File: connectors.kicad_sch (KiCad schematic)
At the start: 4 parts, among them J1 Conn_01x04_Pin, J2 Conn_01x04_Pin, J3 Conn_01x09_Pin, J4 Conn_02x03_Odd_Even

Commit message: Assigned footprints to the components in EESchema.
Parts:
- J1, J2: footprint (none) -> Connector_PinHeader_2.54mm:PinHeader_1x04_P2.54mm_Vertical
- J3: footprint (none) -> Connector_PinHeader_2.54mm:PinHeader_1x09_P2.54mm_Vertical
- J4: footprint (none) -> Connector_PinHeader_2.54mm:PinHeader_2x03_P2.54mm_Vertical
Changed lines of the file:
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@@
 			)
 		)
-		(property "Footprint" ""
+		(property "Footprint" "Connector_PinHeader_2.54mm:PinHeader_2x03_P2.54mm_Vertical"
 			(at 95.25 58.42 0)
 			(effects
@@
 			)
 		)
-		(property "Footprint" ""
+		(property "Footprint" "Connector_PinHeader_2.54mm:PinHeader_1x04_P2.54mm_Vertical"
 			(at 60.96 31.75 0)
 			(effects
@@
 			)
 		)
-		(property "Footprint" ""
+		(property "Footprint" "Connector_PinHeader_2.54mm:PinHeader_1x04_P2.54mm_Vertical"
 			(at 93.98 31.75 0)
 			(effects
@@
 			)
 		)
-		(property "Footprint" ""
+		(property "Footprint" "Connector_PinHeader_2.54mm:PinHeader_1x09_P2.54mm_Vertical"
 			(at 60.96 60.96 0)
 			(effects

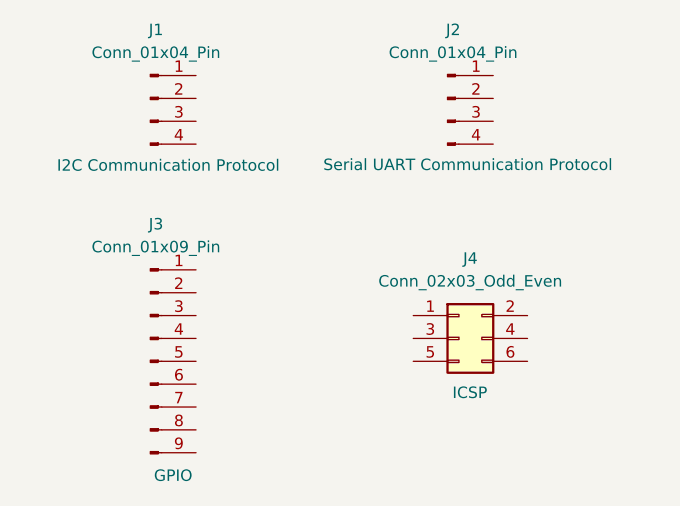
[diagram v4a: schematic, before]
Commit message: Finished the wiring of the schematic.
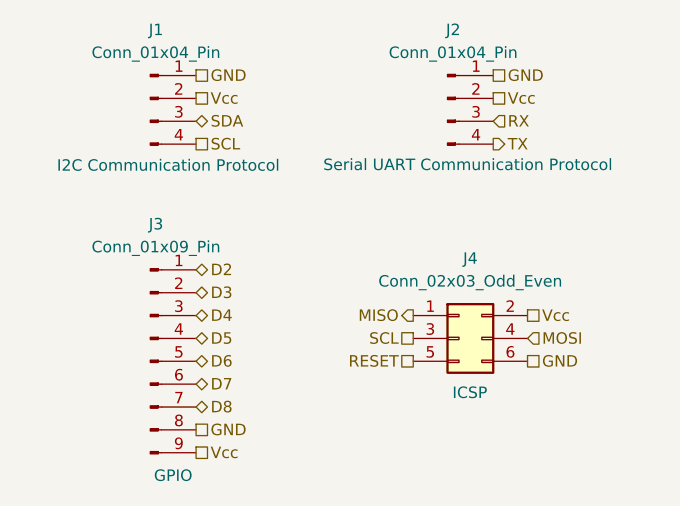
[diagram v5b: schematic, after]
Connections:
- net MISO: now reaches J4.1 (Pin_1)
- net Vcc: now reaches J4.2 (Pin_2)
- net Vcc: now also J1.2 (Pin_2), J2.2 (Pin_2), J3.9 (Pin_9)
- net SCL: now reaches J4.3 (Pin_3)
- net SCL: now also J1.4 (Pin_4)
- net MOSI: now reaches J4.4 (Pin_4)
- net RESET: now reaches J4.5 (Pin_5)
- net GND: now reaches J4.6 (Pin_6)
- net GND: now also J1.1 (Pin_1), J2.1 (Pin_1), J3.8 (Pin_8)
- net SDA: now reaches J1.3 (Pin_3)
- net RX: now reaches J2.3 (Pin_3)
- net TX: now reaches J2.4 (Pin_4)
- net D2: now reaches J3.1 (Pin_1)
- net D3: now reaches J3.2 (Pin_2)
- net D4: now reaches J3.3 (Pin_3)
- net D5: now reaches J3.4 (Pin_4)
- net D6: now reaches J3.5 (Pin_5)
- net D7: now reaches J3.6 (Pin_6)
- net D8: now reaches J3.7 (Pin_7)
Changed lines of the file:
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@@
 	(generator_version "9.0")
 	(paper "A4")
+	(hierarchical_label "D6"
+		(shape bidirectional)
+		(at 66.04 60.96 0)
+		(effects
+			(font
+				(size 1.27 1.27)
+			)
+			(justify left)
+		)
+	)
+	(hierarchical_label "GND"
+		(shape passive)
+		(at 99.06 29.21 0)
+		(effects
+			(font
+				(size 1.27 1.27)
+			)
+			(justify left)
+		)
+	)
+	(hierarchical_label "D2"
+		(shape bidirectional)
+		(at 66.04 50.8 0)
+		(effects
+			(font
+				(size 1.27 1.27)
+			)
+			(justify left)
+		)
+	)
+	(hierarchical_label "GND"
+		(shape passive)
+		(at 66.04 29.21 0)
+		(effects
+			(font
+				(size 1.27 1.27)
+			)
+			(justify left)
+		)
+	)
+	(hierarchical_label "D7"
+		(shape bidirectional)
+		(at 66.04 63.5 0)
+		(effects
+			(font
+				(size 1.27 1.27)
+			)
+			(justify left)
+		)
+	)
+	(hierarchical_label "RESET"
+		(shape passive)
+		(at 90.17 60.96 180)
+		(effects
+			(font
+				(size 1.27 1.27)
+			)
+			(justify right)
+		)
+	)
+	(hierarchical_label "Vcc"
+		(shape passive)
+		(at 99.06 31.75 0)
+		(effects
+			(font
+				(size 1.27 1.27)
+			)
+			(justify left)
+		)
+	)
+	(hierarchical_label "MOSI"
+		(shape input)
+		(at 102.87 58.42 0)
+		(effects
+			(font
+				(size 1.27 1.27)
+			)
+			(justify left)
+		)
+	)
+	(hierarchical_label "Vcc"
+		(shape passive)
+		(at 66.04 71.12 0)
+		(effects
+			(font
+				(size 1.27 1.27)
+			)
+			(justify left)
+		)
+	)
+	(hierarchical_label "SCL"
+		(shape passive)
+		(at 90.17 58.42 180)
+		(effects
+			(font
+				(size 1.27 1.27)
+			)
+			(justify right)
+		)
+	)
+	(hierarchical_label "RX"
+		(shape input)
+		(at 99.06 34.29 0)
+		(effects
+			(font
+				(size 1.27 1.27)
+			)
+			(justify left)
+		)
+	)
+	(hierarchical_label "GND"
+		(shape passive)
+		(at 66.04 68.58 0)
+		(effects
+			(font
+				(size 1.27 1.27)
+			)
+			(justify left)
+		)
+	)
+	(hierarchical_label "SDA"
+		(shape bidirectional)
+		(at 66.04 34.29 0)
+		(effects
+			(font
+				(size 1.27 1.27)
+			)
+			(justify left)
+		)
+	)
+	(hierarchical_label "GND"
+		(shape passive)
+		(at 102.87 60.96 0)
+		(effects
+			(font
+				(size 1.27 1.27)
+			)
+			(justify left)
+		)
+	)
+	(hierarchical_label "D3"
+		(shape bidirectional)
+		(at 66.04 53.34 0)
+		(effects
+			(font
+				(size 1.27 1.27)
+			)
+			(justify left)
+		)
+	)
+	(hierarchical_label "Vcc"
+		(shape passive)
+		(at 102.87 55.88 0)
+		(effects
+			(font
+				(size 1.27 1.27)
+			)
+			(justify left)
+		)
+	)
+	(hierarchical_label "D8"
+		(shape bidirectional)
+		(at 66.04 66.04 0)
+		(effects
+			(font
+				(size 1.27 1.27)
+			)
+			(justify left)
+		)
+	)
+	(hierarchical_label "SCL"
+		(shape passive)
+		(at 66.04 36.83 0)
+		(effects
+			(font
+				(size 1.27 1.27)
+			)
+			(justify left)
+		)
+	)
+	(hierarchical_label "D5"
+		(shape bidirectional)
+		(at 66.04 58.42 0)
+		(effects
+			(font
+				(size 1.27 1.27)
+			)
+			(justify left)
+		)
+	)
+	(hierarchical_label "Vcc"
+		(shape passive)
+		(at 66.04 31.75 0)
+		(effects
+			(font
+				(size 1.27 1.27)
+			)
+			(justify left)
+		)
+	)
+	(hierarchical_label "TX"
+		(shape output)
+		(at 99.06 36.83 0)
+		(effects
+			(font
+				(size 1.27 1.27)
+			)
+			(justify left)
+		)
+	)
+	(hierarchical_label "D4"
+		(shape bidirectional)
+		(at 66.04 55.88 0)
+		(effects
+			(font
+				(size 1.27 1.27)
+			)
+			(justify left)
+		)
+	)
+	(hierarchical_label "MISO"
+		(shape output)
+		(at 90.17 55.88 180)
+		(effects
+			(font
+				(size 1.27 1.27)
+			)
+			(justify right)
+		)
+	)
 	(symbol
 		(lib_id "Connector_Generic:Conn_02x03_Odd_Even")

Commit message: Fixed the problem with the clock signal. I've added SCK for the clock signal of SPI commmunication protocol.
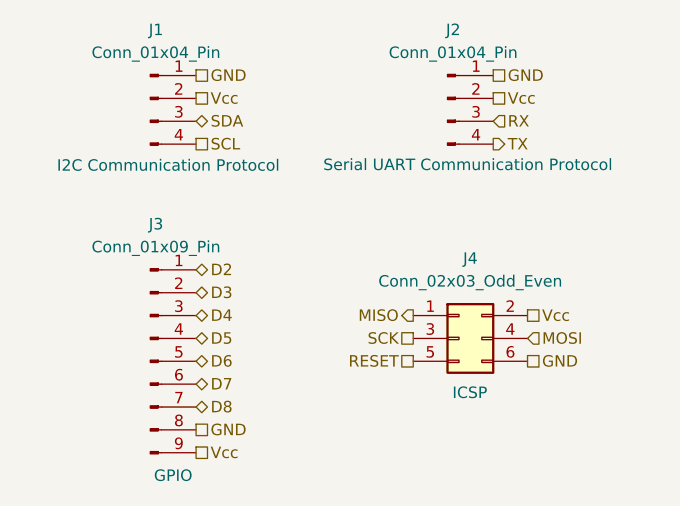
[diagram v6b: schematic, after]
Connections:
- net SCL: no longer J4.3 (Pin_3)
- new net SCK: J4.3 (Pin_3)
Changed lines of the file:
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@@
 		)
 	)
-	(hierarchical_label "SCL"
+	(hierarchical_label "SCK"
 		(shape passive)
 		(at 90.17 58.42 180)
